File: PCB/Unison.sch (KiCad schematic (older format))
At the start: 262 parts, among them J1 USB4085-GF-A_REVA, J2 Conn_02x05_Odd_Even, U1 ATmega32U4-AU, Y1 16MHz

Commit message: Update: ICSP仮配置
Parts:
- removed OL1: OLED, ukiha:OLED_rev2, symbol swanmatch:OLED
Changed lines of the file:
@@
 	1    0    0    -1
 $EndComp
-$Comp
-L power:+5V #PWR026
-U 1 1 5F1DDB61
-P 12950 9450
-F 0 "#PWR026" H 12950 9300 50  0001 C CNN
-F 1 "+5V" H 12965 9623 50  0000 C CNN
-F 2 "" H 12950 9450 50  0001 C CNN
-F 3 "" H 12950 9450 50  0001 C CNN
-	1    12950 9450
-	1    0    0    -1
-$EndComp
-Wire Wire Line
-	13525 9450 12950 9450
 Wire Wire Line
 	13450 7075 13900 7075
@@
 Text GLabel 11050 2650 1    50   Input ~ 0
 RE5_2
-$Comp
-L power:GND #PWR029
-U 1 1 5F1DF82B
-P 13525 9600
-F 0 "#PWR029" H 13525 9350 50  0001 C CNN
-F 1 "GND" H 13530 9427 50  0000 C CNN
-F 2 "" H 13525 9600 50  0001 C CNN
-F 3 "" H 13525 9600 50  0001 C CNN
-	1    13525 9600
-	1    0    0    -1
-$EndComp
 Wire Wire Line
 	10650 7425 11300 7425
@@
 Text GLabel 2825 10800 2    50   Input ~ 0
 RE2_A
-Text GLabel 13525 9300 0    50   Input ~ 0
-SCL
-Text GLabel 13525 9150 0    50   Input ~ 0
-SDA
 Wire Notes Line
 	5575 9250 5575 9200
@@
 	10650 1325 10650 2225
 $Comp
-L swanmatch:OLED OL1
-U 1 1 62544862
-P 14275 9400
-F 0 "OL1" H 14903 9469 51  0000 L CNN
-F 1 "OLED" H 14903 9379 47  0000 L CNN
-F 2 "ukiha:OLED_rev2" H 14275 9500 60  0001 C CNN
-F 3 "" H 14275 9500 60  0001 C CNN
-	1    14275 9400
-	1    0    0    -1
-$EndComp
-$Comp
 L power:+5V #PWR06

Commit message: Update: 組立時、1uフットプリント兼用の2uキーの場所がわかりにくいため、2uフットプリントに変更し、シルクで判別できるようにした。
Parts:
- SW_35_1, SW_45_1, SW_65_1, SW_75_1: footprint ukiha:CherryMX_MidHeight_16mm_rev2 -> ukiha:CherryMX_MidHeight_16mm_rev2_2u_guide
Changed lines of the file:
@@
 F 0 "SW_35_1" H 4350 8110 50  0000 C CNN
 F 1 "SW_Push" H 4350 8019 50  0000 C CNN
-F 2 "ukiha:CherryMX_MidHeight_16mm_rev2" H 4350 8025 50  0001 C CNN
+F 2 "ukiha:CherryMX_MidHeight_16mm_rev2_2u_guide" H 4350 8025 50  0001 C CNN
 F 3 "~" H 4350 8025 50  0001 C CNN
 	1    4350 7825
@@
 F 0 "SW_45_1" H 5650 8110 50  0000 C CNN
 F 1 "SW_Push" H 5650 8019 50  0000 C CNN
-F 2 "ukiha:CherryMX_MidHeight_16mm_rev2" H 5650 8025 50  0001 C CNN
+F 2 "ukiha:CherryMX_MidHeight_16mm_rev2_2u_guide" H 5650 8025 50  0001 C CNN
 F 3 "~" H 5650 8025 50  0001 C CNN
 	1    5650 7825
@@
 F 0 "SW_75_1" H 8250 8110 50  0000 C CNN
 F 1 "SW_Push" H 8250 8019 50  0000 C CNN
-F 2 "ukiha:CherryMX_MidHeight_16mm_rev2" H 8250 8025 50  0001 C CNN
+F 2 "ukiha:CherryMX_MidHeight_16mm_rev2_2u_guide" H 8250 8025 50  0001 C CNN
 F 3 "~" H 8250 8025 50  0001 C CNN
 	1    8250 7825
@@
 F 0 "SW_65_1" H 6950 8110 50  0000 C CNN
 F 1 "SW_Push" H 6950 8019 50  0000 C CNN
-F 2 "ukiha:CherryMX_MidHeight_16mm_rev2" H 6950 8025 50  0001 C CNN
+F 2 "ukiha:CherryMX_MidHeight_16mm_rev2_2u_guide" H 6950 8025 50  0001 C CNN
 F 3 "~" H 6950 8025 50  0001 C CNN
 	1    6950 7825

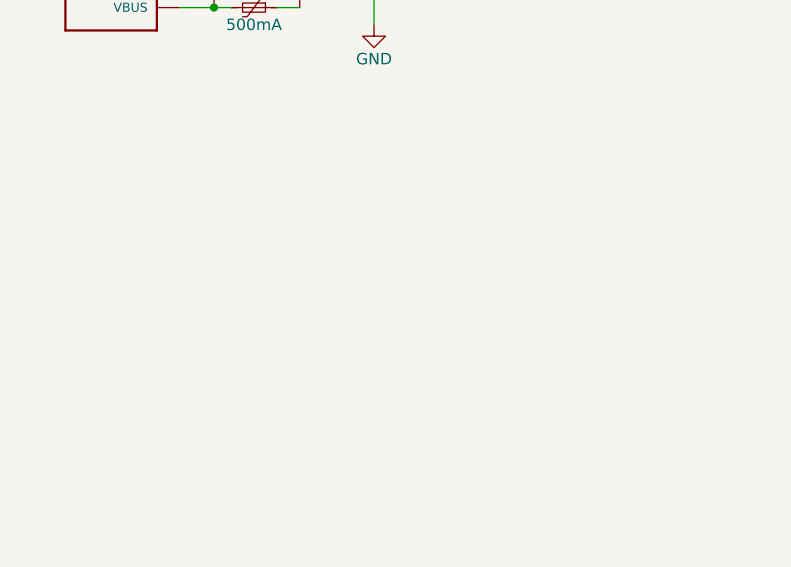
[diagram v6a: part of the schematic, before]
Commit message: Update: ネジ穴かぶるスイッチのフットプリントをMill-maxソケットが使用できるものへ変更。LED光線もれ防止追加。
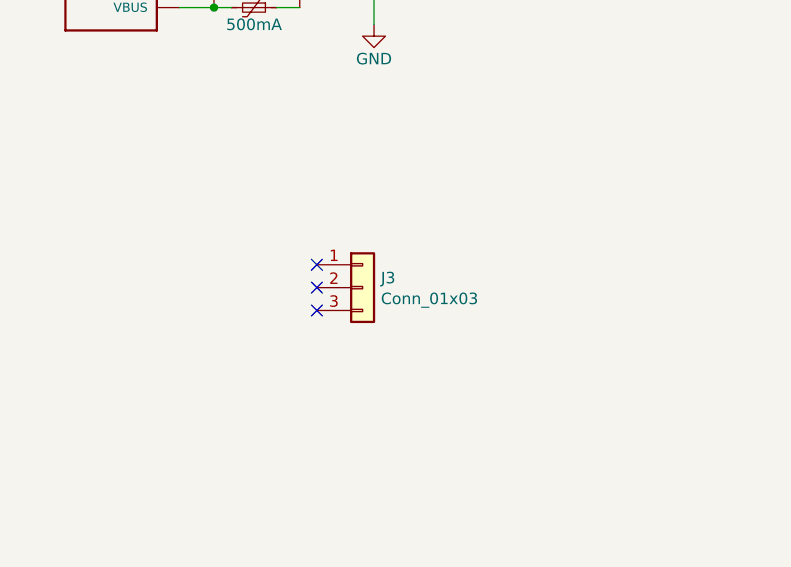
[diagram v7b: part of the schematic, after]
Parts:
- added J3: Conn_01x03, Connector_PinSocket_2.54mm:PinSocket_1x03_P2.54mm_Vertical, symbol Connector_Generic:Conn_01x03
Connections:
- no-connect marks 6 -> 9
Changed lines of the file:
@@
 Text GLabel 12875 6100 0    50   Input ~ 0
 AUDIO
+$Comp
+L Connector_Generic:Conn_01x03 J3
+U 1 1 60D2854A
+P 14250 9400
+F 0 "J3" H 14330 9442 50  0000 L CNN
+F 1 "Conn_01x03" H 14330 9351 50  0000 L CNN
+F 2 "Connector_PinSocket_2.54mm:PinSocket_1x03_P2.54mm_Vertical" H 14250 9400 50  0001 C CNN
+F 3 "~" H 14250 9400 50  0001 C CNN
+	1    14250 9400
+	1    0    0    -1
+$EndComp
+NoConn ~ 14050 9300
+NoConn ~ 14050 9400
+NoConn ~ 14050 9500
 $EndSCHEMATC

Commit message: Update: ネジ穴かぶるスイッチのフットプリントをMill-maxソケットが使用できるものへ変更。LED光線もれ防止追加。
ファイル追加忘れ
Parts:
- SW_18_1, SW_21, SW_53, SW_8_1, SW_91: footprint ukiha:CherryMX_MidHeight_16mm_rev2 -> ukiha:MXOnly-1U-NoLED_16mm
- SW_60_3, SW_75_1: footprint ukiha:CherryMX_MidHeight_16mm_rev2_2u_guide -> ukiha:MXOnly-2U-NoLED_16mm
- SW_75_2: footprint ukiha:CherryMX_MidHeight_16mm_rev2_1.5u_guide -> ukiha:MXOnly-1.5U-NoLED_16mm
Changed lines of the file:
@@
 F 0 "SW_21" H 1750 3110 50  0000 C CNN
 F 1 "SW_Push" H 1750 3019 50  0000 C CNN
-F 2 "ukiha:CherryMX_MidHeight_16mm_rev2" H 1750 3025 50  0001 C CNN
+F 2 "ukiha:MXOnly-1U-NoLED_16mm" H 1750 3025 50  0001 C CNN
 F 3 "~" H 1750 3025 50  0001 C CNN
 	1    1750 2825
@@
 F 0 "SW_18_1" H 1100 5610 50  0000 C CNN
 F 1 "SW_Push" H 1100 5519 50  0000 C CNN
-F 2 "ukiha:CherryMX_MidHeight_16mm_rev2" H 1100 5525 50  0001 C CNN
+F 2 "ukiha:MXOnly-1U-NoLED_16mm" H 1100 5525 50  0001 C CNN
 F 3 "~" H 1100 5525 50  0001 C CNN
 	1    1100 5325
@@
 F 0 "SW_53" H 5650 5610 50  0000 C CNN
 F 1 "SW_Push" H 5650 5519 50  0000 C CNN
-F 2 "ukiha:CherryMX_MidHeight_16mm_rev2" H 5650 5525 50  0001 C CNN
+F 2 "ukiha:MXOnly-1U-NoLED_16mm" H 5650 5525 50  0001 C CNN
 F 3 "~" H 5650 5525 50  0001 C CNN
 	1    5650 5325
@@
 F 0 "SW_75_1" H 8250 8110 50  0000 C CNN
 F 1 "SW_Push" H 8250 8019 50  0000 C CNN
-F 2 "ukiha:CherryMX_MidHeight_16mm_rev2_2u_guide" H 8250 8025 50  0001 C CNN
+F 2 "ukiha:MXOnly-2U-NoLED_16mm" H 8250 8025 50  0001 C CNN
 F 3 "~" H 8250 8025 50  0001 C CNN
 	1    8250 7825
@@
 F 0 "SW_91" H 10850 3110 50  0000 C CNN
 F 1 "SW_Push" H 10850 3019 50  0000 C CNN
-F 2 "ukiha:CherryMX_MidHeight_16mm_rev2" H 10850 3025 50  0001 C CNN
+F 2 "ukiha:MXOnly-1U-NoLED_16mm" H 10850 3025 50  0001 C CNN
 F 3 "~" H 10850 3025 50  0001 C CNN
 	1    10850 2825
@@
 F 0 "SW_8_1" H 11500 5610 50  0000 C CNN
 F 1 "SW_Push" H 11500 5519 50  0000 C CNN
-F 2 "ukiha:CherryMX_MidHeight_16mm_rev2" H 11500 5525 50  0001 C CNN
+F 2 "ukiha:MXOnly-1U-NoLED_16mm" H 11500 5525 50  0001 C CNN
 F 3 "~" H 11500 5525 50  0001 C CNN
 F 4 "SW_08" H 11500 5900 50  0000 C CNN "Alt Ref"
@@
 F 0 "SW_75_2" H 8250 7935 50  0000 C CNN
 F 1 "SW_Push" H 8250 7844 50  0000 C CNN
-F 2 "ukiha:CherryMX_MidHeight_16mm_rev2_1.5u_guide" H 8250 7850 50  0001 C CNN
+F 2 "ukiha:MXOnly-1.5U-NoLED_16mm" H 8250 7850 50  0001 C CNN
 F 3 "~" H 8250 7850 50  0001 C CNN
 	1    8250 7650
@@
 F 0 "SW_60_3" H 7600 7760 50  0000 C CNN
 F 1 "SW_Push" H 7600 7669 50  0000 C CNN
-F 2 "ukiha:CherryMX_MidHeight_16mm_rev2_2u_guide" H 7600 7675 50  0001 C CNN
+F 2 "ukiha:MXOnly-2U-NoLED_16mm" H 7600 7675 50  0001 C CNN
 F 3 "~" H 7600 7675 50  0001 C CNN
 	1    7600 7475
